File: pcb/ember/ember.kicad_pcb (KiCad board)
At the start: 2 copper layers, 139 x 113.5 mm, 102 parts, among them IC1 ADG708BRUZ-REEL7, IC2 ADG708BRUZ-REEL7, IC3 ADG708BRUZ-REEL7, IC4 ADG708BRUZ-REEL7, IC5 M24C64-RMN6TP, J2 USB_C_Receptacle_USB2.0, J3 Conn_01x05_Socket, SW1 RESET, SW2 BOOT, U1 Hall_Sensor, U10 Hall_Sensor, U11 Hall_Sensor, U12 Hall_Sensor, U13 Hall_Sensor, U14 Hall_Sensor, U15 Hall_Sensor, U16 Hall_Sensor, U17 Hall_Sensor, U18 Hall_Sensor, U19 Hall_Sensor, U2 Hall_Sensor, U20 Hall_Sensor, U21 Hall_Sensor, U22 Hall_Sensor, U23 Hall_Sensor, U24 Hall_Sensor, U25 Hall_Sensor, U26 Hall_Sensor, U27 Hall_Sensor, U28 Hall_Sensor, U29 Hall_Sensor, U3 Hall_Sensor, U30 Hall_Sensor, U31 Hall_Sensor, U32 Hall_Sensor, U33 AMS1117-3.3, U34 SRV05-4, U4 Hall_Sensor, U5 Hall_Sensor, U6 Hall_Sensor, U7 Hall_Sensor, U8 Hall_Sensor, U9 Hall_Sensor, Y1 16MHz

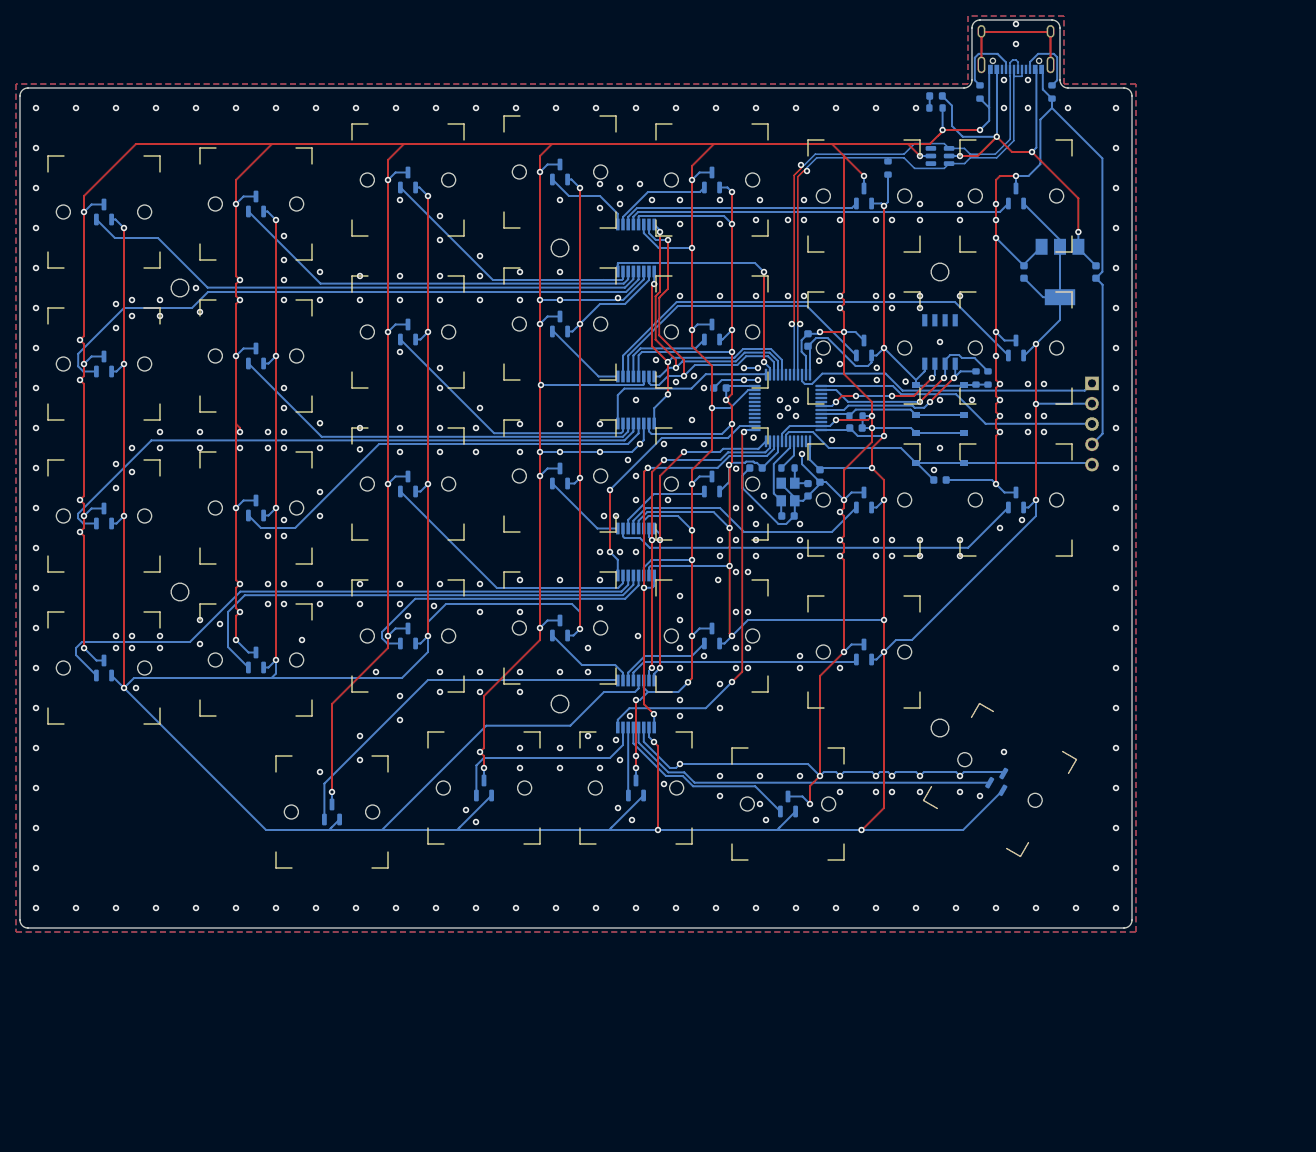
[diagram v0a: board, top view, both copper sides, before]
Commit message: :sparkles: add bypass cap
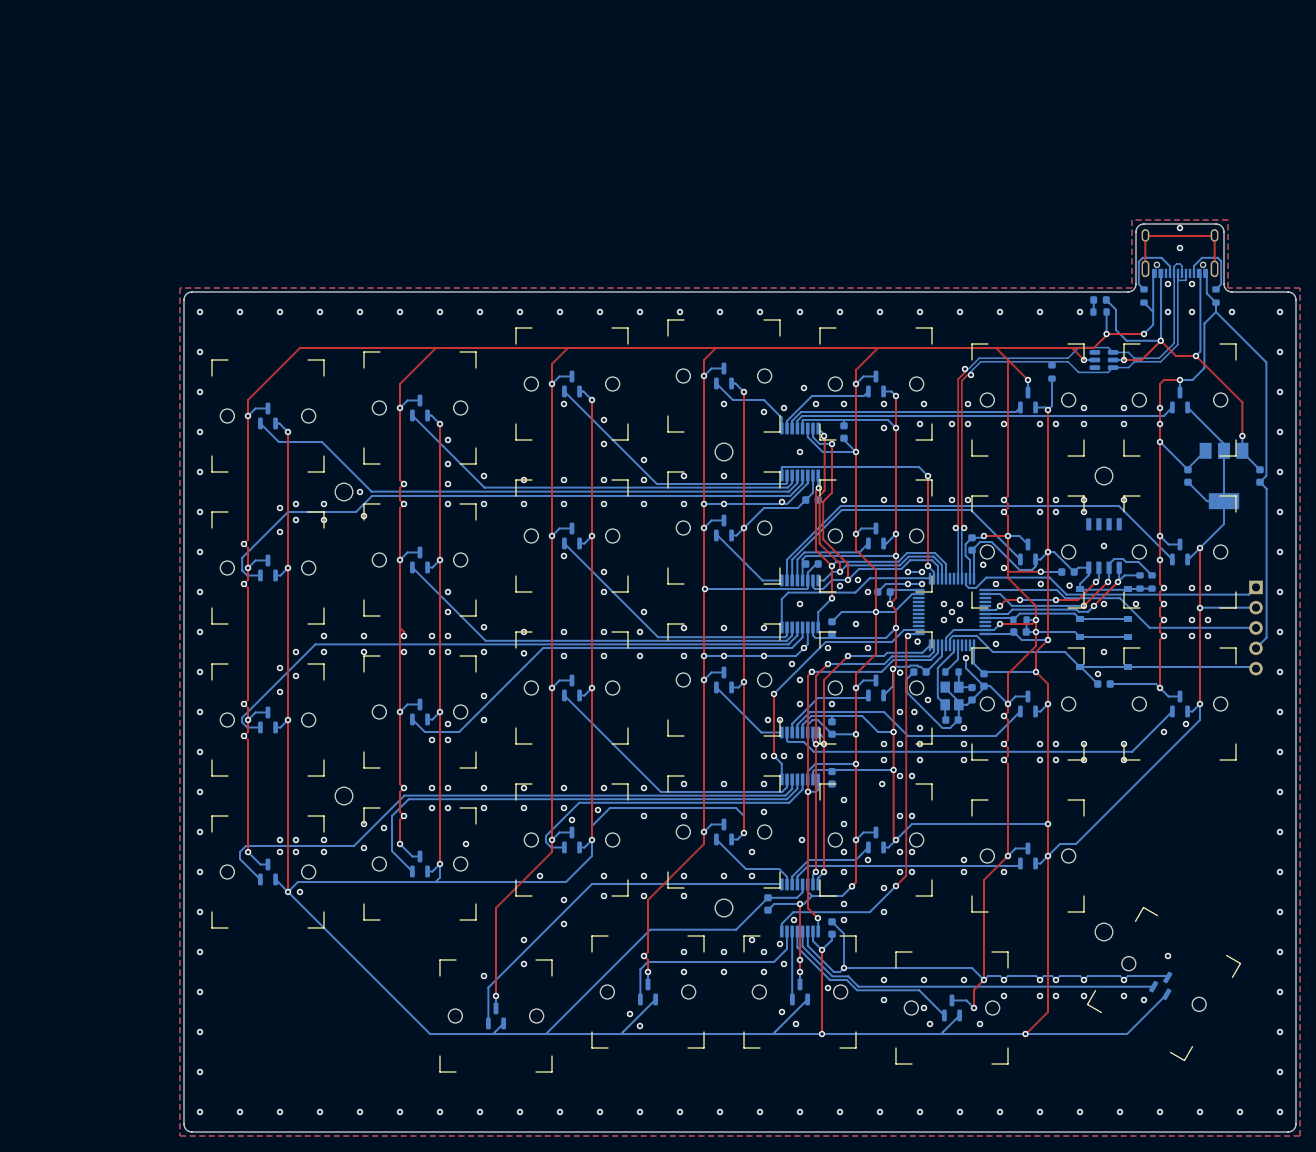
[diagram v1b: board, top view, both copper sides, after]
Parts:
- added C12: 100n, Capacitor_SMD:C_0603_1608Metric, B.Cu at (132.5, 67.5)
- added C13: 100n, Capacitor_SMD:C_0603_1608Metric, B.Cu at (128.5, 76.0)
- added C14: 100n, Capacitor_SMD:C_0603_1608Metric, B.Cu at (128.5, 84.0)
- added C15: 100n, Capacitor_SMD:C_0603_1608Metric, B.Cu at (131.0, 92.0)
- added C16: 100n, Capacitor_SMD:C_0603_1608Metric, B.Cu at (131.0, 104.5)
- added C17: 100n, Capacitor_SMD:C_0603_1608Metric, B.Cu at (131.0, 110.7)
- added C18: 100n, Capacitor_SMD:C_0603_1608Metric, B.Cu at (123.0, 126.5)
- added C19: 100n, Capacitor_SMD:C_0603_1608Metric, B.Cu at (131.0, 129.5)
- added C8: 100n, Capacitor_SMD:C_0603_1608Metric, B.Cu at (160.5, 85.0)
- moved C1 32.7 mm to (148.5, 81.5)
- moved C10 32.7 mm to (175.5, 73.0)
- moved C11 32.7 mm to (165.0, 99.0)
- moved C2 32.7 mm to (154.5, 92.5)
- moved C3 32.7 mm to (150.0, 98.5)
- moved C4 32.7 mm to (137.5, 87.5)
- moved C5 32.7 mm to (142.0, 97.5)
- moved C6 32.7 mm to (148.5, 100.2)
- moved C7 32.7 mm to (146.0, 103.5)
- moved C9 32.7 mm to (184.5, 73.0)
- moved D1 32.7 mm to (164.5, 51.0)
- moved H1 32.7 mm to (70.0, 75.0)
- moved H10 32.7 mm to (117.5, 60.5)
- moved H11 32.7 mm to (136.5, 61.5)
- moved H12 32.7 mm to (155.5, 63.5)
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- renumbered C3 to C1, C1 to C10, C4 to C2, C5 to C3, C6 to C4, C7 to C5, C9 to C6, C10 to C7, C2 to C9, D2 to D1, H33 to H1, H4 to H10, H5 to H11, H6 to H12, H7 to H13, H8 to H14, H9 to H15, H10 to H16, H11 to H17, H12 to H18, H13 to H19, H36 to H2, H14 to H20, H15 to H21, H16 to H22, H17 to H23, H18 to H24, H19 to H25, H20 to H26, H21 to H27, H22 to H28, H23 to H29, H34 to H3, H24 to H30, H25 to H31, H26 to H32, H27 to H33, H28 to H34, H29 to H35, H30 to H36, H31 to H37, H32 to H38, H37 to H4, H35 to H5, H38 to H6, H1 to H7, H2 to H8, H3 to H9, IC5 to IC1, IC1 to IC2, IC2 to IC3, IC3 to IC4, IC4 to IC5, J2 to J1, J3 to J2, R8 to R3, R3 to R4, R7 to R5, R5 to R7, R4 to R8, SW2 to SW1, SW1 to SW2, U34 to U1, U29 to U10, U2 to U11, U6 to U12, U10 to U13, U18 to U15, U22 to U16, U26 to U17, U30 to U18, U3 to U19, U33 to U2, U7 to U20, U11 to U21, U15 to U22, U19 to U23, U23 to U24, U27 to U25, U31 to U26, U4 to U27, U8 to U28, U12 to U29, U1 to U3, U16 to U30, U20 to U31, U24 to U32, U28 to U33, U32 to U34, U5 to U4, U9 to U5, U13 to U6, U17 to U7, U21 to U8, U25 to U9
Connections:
- net SENS_A_CH0 renamed SENS_A_S2
- net SENS_A_CH1 renamed SENS_A_S3
- net SENS_A_CH2 renamed SENS_A_S4
- net SENS_A_CH3 renamed SENS_A_S1
- net SENS_A_CH4 renamed SENS_A_S8
- net SENS_A_CH5 renamed SENS_A_S5
- net SENS_A_CH6 renamed SENS_A_S7
- net SENS_A_CH7 renamed SENS_A_S6
- net SENS_B_CH0 renamed SENS_B_S2
- net SENS_B_CH1 renamed SENS_B_S3
- net SENS_B_CH2 renamed SENS_B_S4
- net SENS_B_CH3 renamed SENS_B_S1
- net SENS_B_CH4 renamed SENS_B_S8
- net SENS_B_CH5 renamed SENS_B_S5
- net SENS_B_CH6 renamed SENS_B_S7
- net SENS_B_CH7 renamed SENS_B_S6
- net SENS_C_CH0 renamed SENS_C_S2
- net SENS_C_CH1 renamed SENS_C_S3
- net SENS_C_CH2 renamed SENS_C_S4
- net SENS_C_CH3 renamed SENS_C_S1
- net SENS_C_CH4 renamed SENS_C_S8
- net SENS_C_CH5 renamed SENS_C_S5
- net SENS_C_CH6 renamed SENS_C_S7
- net SENS_C_CH7 renamed SENS_C_S6
- net SENS_D_CH0 renamed SENS_D_S2
- net SENS_D_CH1 renamed SENS_D_S3
- net SENS_D_CH2 renamed SENS_D_S4
- net SENS_D_CH3 renamed SENS_D_S1
- net SENS_D_CH4 renamed SENS_D_S8
- net SENS_D_CH5 renamed SENS_D_S5
- net SENS_D_CH6 renamed SENS_D_S7
- net SENS_D_CH7 renamed SENS_D_S6
- IC4 pad 15: MUX1_B -> MUX1_C
- IC4 pad 16: MUX1_C -> MUX1_B
- IC5 pad 15: MUX1_B -> MUX1_C
- IC5 pad 16: MUX1_C -> MUX1_B
- MCU1 pad 11: MUX1_B -> MUX1_C
- MCU1 pad 12: MUX1_C -> MUX1_B
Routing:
- net GND: track 1015.0 -> 1043.6 mm, vias 449 -> 445
- net +3.3V: track 917.2 -> 923.4 mm
- net MUX1_B: track 44.6 -> 42.7 mm
- net MUX1_C: track 42.7 -> 44.6 mm

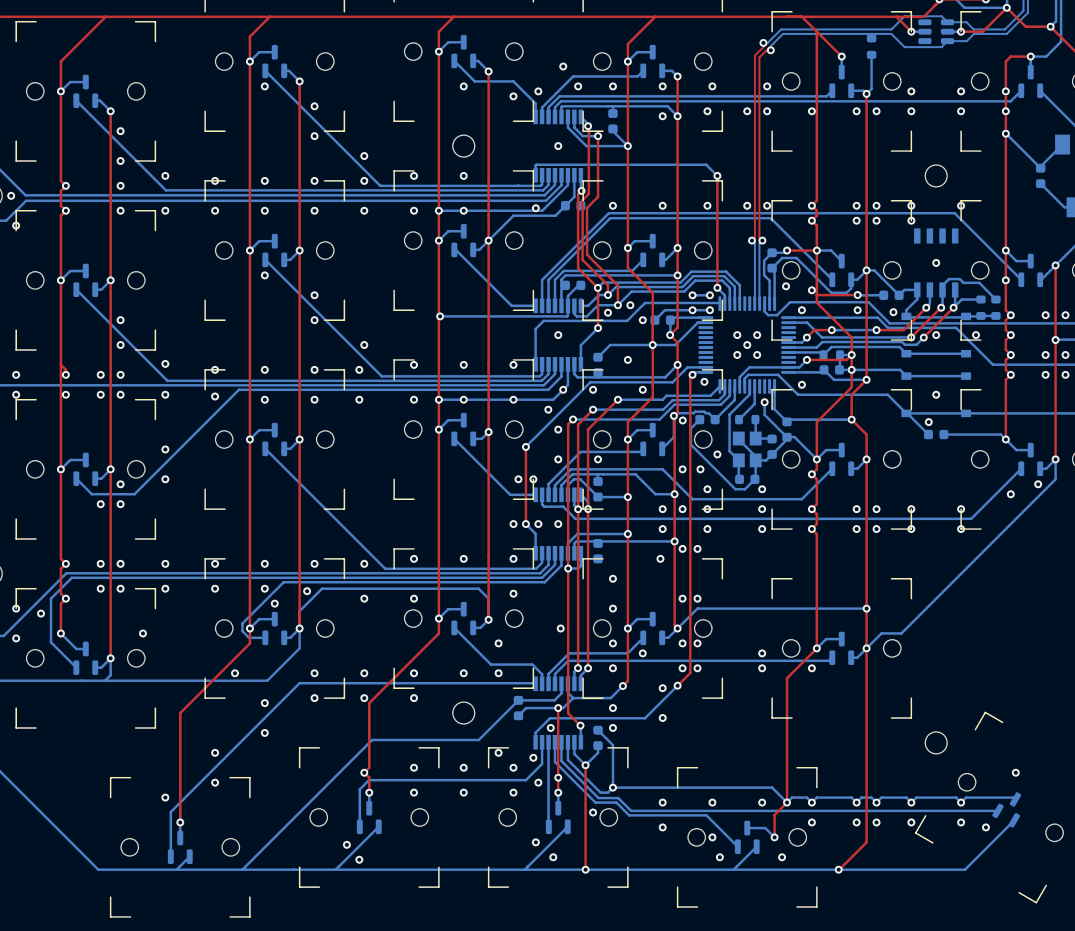
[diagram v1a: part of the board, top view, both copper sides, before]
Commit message: :sparkles: opampを使ってのADCに切り替えられるようにピンアサインを変更
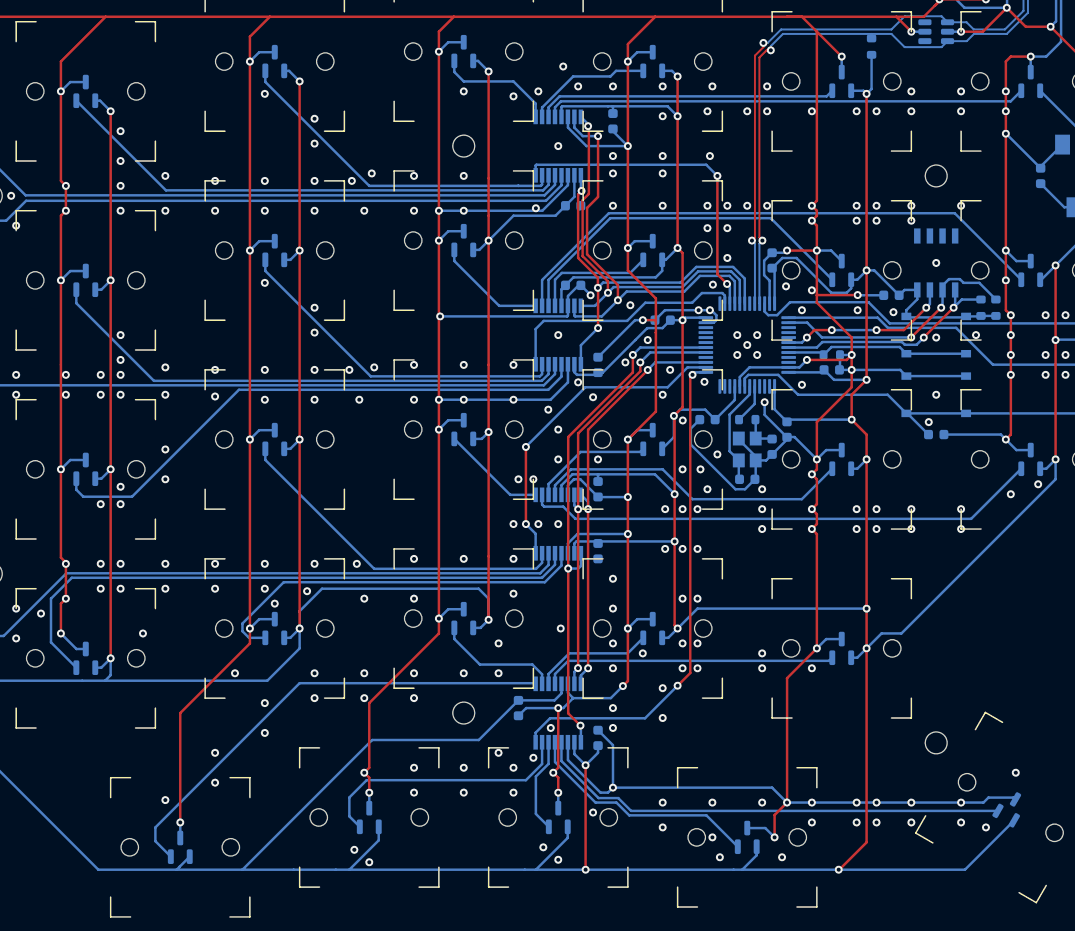
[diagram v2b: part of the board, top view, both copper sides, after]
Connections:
- IC2 pad 8: ADC3 -> ADC4
- IC3 pad 8: ADC4 -> ADC3
- MCU1 pad 10: MUX1_A -> unconnected-(MCU1-PA0-Pad10)
- MCU1 pad 11: MUX1_C -> unconnected-(MCU1-PA1-Pad11)
- MCU1 pad 12: MUX1_B -> /OMAMP1_VOUT
- MCU1 pad 15: unconnected-(MCU1-PA5-Pad15) -> MUX1_B
- MCU1 pad 16: unconnected-(MCU1-PA6-Pad16) -> /OMAMP2_VOUT
- MCU1 pad 17: unconnected-(MCU1-PA7-Pad17) -> MUX1_C
- MCU1 pad 18: unconnected-(MCU1-PB0-Pad18) -> MUX1_A
- MCU1 pad 19: unconnected-(MCU1-PB1-Pad19) -> /OMAMP3_VOUT
- MCU1 pad 25: ADC4 -> /OMAMP4_VOUT
- MCU1 pad 27: MUX2_C -> ADC4
- MCU1 pad 28: MUX2_B -> MUX2_C
- MCU1 pad 29: MUX2_A -> MUX2_B
- MCU1 pad 30: unconnected-(MCU1-PA9-Pad30) -> MUX2_A
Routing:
- net ADC4: track 23.2 -> 33.1 mm, vias 0 -> 2
- net GND: track 1043.6 -> 1034.6 mm, vias 445 -> 451
- net ADC3: track 32.9 -> 25.0 mm, vias 2 -> 0
- net +3.3V: track 923.4 -> 919.6 mm, vias 39 -> 37
- net MUX2_A: track 38.1 -> 39.4 mm
- net SENS_D_S8: track 46.6 -> 47.8 mm
- net MUX2_B: track 38.4 -> 39.5 mm
- net MUX1_A: track 53.5 -> 52.5 mm
- net SENS_D_S3: track 8.51 -> 9.57 mm
- net SENS_D_S4: track 25.3 -> 26.3 mm
- net MUX1_C: track 44.6 -> 43.7 mm
- net MUX2_C: track 42.5 -> 43.4 mm
- net SENS_B_S1: track 55.6 -> 56.4 mm
- net SENS_B_S3: track 52.5 -> 53.3 mm
- net SENS_C_S4: track 34.0 -> 34.7 mm
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
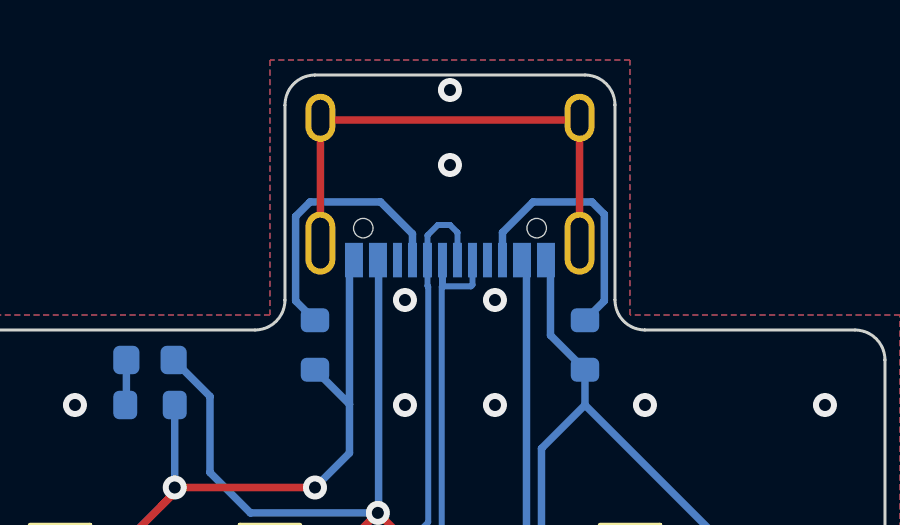
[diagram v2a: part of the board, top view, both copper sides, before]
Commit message: :sparkles: add usb logo
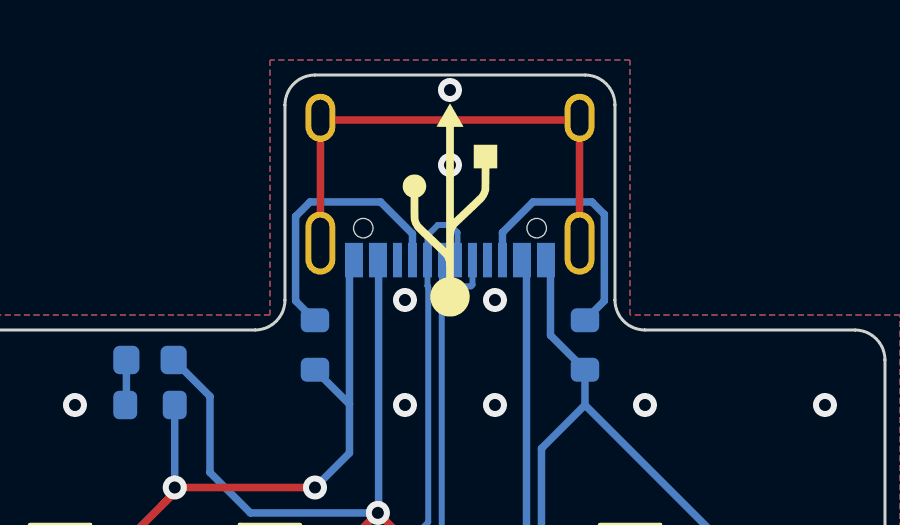
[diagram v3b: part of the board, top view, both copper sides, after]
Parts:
- added G***: LOGO, ember:usb_logo, F.Cu at (174.5, 46.0)
